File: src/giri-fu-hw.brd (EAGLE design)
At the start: 91.1 x 54.6 mm, 30 parts, among them IC1 ATMEGA168-20P, IC2 7805T, IC3 ULN2003AN, K1 G5V1, K2 G5V1, K3 G5V1, K4 G5V1, K5 G5V1, K6 G5V1, Q1 16MHz

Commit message: Rename inputs and outputs Regenerate dist artifacts
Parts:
- renumbered X10 to SWITCH_1, X11 to SWITCH_2, X12 to SWITCH_3, X13 to SWITCH_4, X14 to SWITCH_5, X15 to SWITCH_6, X16 to 24VAC_IN, X17 to 12VAC_IN
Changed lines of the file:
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@@
 <element name="D4" library="diode" package="DO41-10" value="1N4004" x="17.78" y="20.32" rot="R180"/>
 <element name="C5" library="rcl" package="E35-12" value="" x="24.13" y="34.29" rot="R180"/>
-<element name="X10" library="con-wago-508" package="W237-132" value="" x="81.28" y="5.08" rot="R180">
+<element name="SWITCH_1" library="con-wago-508" package="W237-132" value="" x="81.28" y="5.08" rot="R180">
 <attribute name="OC_NEWARK" value="unknown" x="81.28" y="5.08" size="1.778" layer="27" rot="R180" display="off"/>
 <attribute name="MPN" value="" x="81.28" y="5.08" size="1.778" layer="27" rot="R180" display="off"/>
@@
 <attribute name="OC_FARNELL" value="unknown" x="81.28" y="5.08" size="1.778" layer="27" rot="R180" display="off"/>
 </element>
-<element name="X11" library="con-wago-508" package="W237-132" value="" x="71.12" y="5.08" rot="R180">
+<element name="SWITCH_2" library="con-wago-508" package="W237-132" value="" x="71.12" y="5.08" rot="R180">
 <attribute name="OC_NEWARK" value="unknown" x="71.12" y="5.08" size="1.778" layer="27" rot="R180" display="off"/>
 <attribute name="MPN" value="" x="71.12" y="5.08" size="1.778" layer="27" rot="R180" display="off"/>
@@
 <attribute name="OC_FARNELL" value="unknown" x="71.12" y="5.08" size="1.778" layer="27" rot="R180" display="off"/>
 </element>
-<element name="X12" library="con-wago-508" package="W237-132" value="" x="60.96" y="5.08" rot="R180">
+<element name="SWITCH_3" library="con-wago-508" package="W237-132" value="" x="60.96" y="5.08" rot="R180">
 <attribute name="OC_NEWARK" value="unknown" x="60.96" y="5.08" size="1.778" layer="27" rot="R180" display="off"/>
 <attribute name="MPN" value="" x="60.96" y="5.08" size="1.778" layer="27" rot="R180" display="off"/>
@@
 <attribute name="OC_FARNELL" value="unknown" x="60.96" y="5.08" size="1.778" layer="27" rot="R180" display="off"/>
 </element>
-<element name="X13" library="con-wago-508" package="W237-132" value="" x="50.8" y="5.08" rot="R180">
+<element name="SWITCH_4" library="con-wago-508" package="W237-132" value="" x="50.8" y="5.08" rot="R180">
 <attribute name="OC_NEWARK" value="unknown" x="50.8" y="5.08" size="1.778" layer="27" rot="R180" display="off"/>
 <attribute name="MPN" value="" x="50.8" y="5.08" size="1.778" layer="27" rot="R180" display="off"/>
@@
 <attribute name="OC_FARNELL" value="unknown" x="50.8" y="5.08" size="1.778" layer="27" rot="R180" display="off"/>
 </element>
-<element name="X14" library="con-wago-508" package="W237-132" value="" x="40.64" y="5.08" rot="R180">
+<element name="SWITCH_5" library="con-wago-508" package="W237-132" value="" x="40.64" y="5.08" rot="R180">
 <attribute name="OC_NEWARK" value="unknown" x="40.64" y="5.08" size="1.778" layer="27" rot="R180" display="off"/>
 <attribute name="MPN" value="" x="40.64" y="5.08" size="1.778" layer="27" rot="R180" display="off"/>
@@
 <attribute name="OC_FARNELL" value="unknown" x="40.64" y="5.08" size="1.778" layer="27" rot="R180" display="off"/>
 </element>
-<element name="X15" library="con-wago-508" package="W237-132" value="" x="30.48" y="5.08" rot="R180">
+<element name="SWITCH_6" library="con-wago-508" package="W237-132" value="" x="30.48" y="5.08" rot="R180">
 <attribute name="OC_NEWARK" value="unknown" x="30.48" y="5.08" size="1.778" layer="27" rot="R180" display="off"/>
 <attribute name="MPN" value="" x="30.48" y="5.08" size="1.778" layer="27" rot="R180" display="off"/>
@@
 <attribute name="OC_FARNELL" value="unknown" x="30.48" y="5.08" size="1.778" layer="27" rot="R180" display="off"/>
 </element>
-<element name="X16" library="con-wago-508" package="W237-132" value="" x="20.32" y="5.08" rot="R180">
+<element name="24VAC_IN" library="con-wago-508" package="W237-132" value="" x="20.32" y="5.08" rot="R180">
 <attribute name="OC_NEWARK" value="unknown" x="20.32" y="5.08" size="1.778" layer="27" rot="R180" display="off"/>
 <attribute name="MPN" value="" x="20.32" y="5.08" size="1.778" layer="27" rot="R180" display="off"/>
@@
 <attribute name="OC_FARNELL" value="unknown" x="20.32" y="5.08" size="1.778" layer="27" rot="R180" display="off"/>
 </element>
-<element name="X17" library="con-wago-508" package="W237-132" value="" x="10.16" y="5.08" rot="R180">
+<element name="12VAC_IN" library="con-wago-508" package="W237-132" value="" x="10.16" y="5.08" rot="R180">
 <attribute name="OC_NEWARK" value="unknown" x="10.16" y="5.08" size="1.778" layer="27" rot="R180" display="off"/>
 <attribute name="MPN" value="" x="10.16" y="5.08" size="1.778" layer="27" rot="R180" display="off"/>
@@
 <contactref element="K2" pad="6"/>
 <contactref element="K2" pad="5"/>
-<contactref element="X16" pad="2"/>
+<contactref element="24VAC_IN" pad="2"/>
 <wire x1="27.94" y1="21.59" x2="33.02" y2="21.59" width="1.27" layer="16"/>
 <wire x1="33.02" y1="21.59" x2="34.29" y2="20.32" width="1.27" layer="16"/>
@@
 <contactref element="D4" pad="A"/>
 <contactref element="D1" pad="C"/>
-<contactref element="X17" pad="1"/>
+<contactref element="12VAC_IN" pad="1"/>
 <wire x1="12.7" y1="20.32" x2="12.7" y2="12.7" width="1.27" layer="16"/>
 <wire x1="12.7" y1="12.7" x2="12.7" y2="5.715" width="1.27" layer="16"/>
@@
 <contactref element="D3" pad="A"/>
 <contactref element="D2" pad="C"/>
-<contactref element="X17" pad="2"/>
+<contactref element="12VAC_IN" pad="2"/>
 <wire x1="7.62" y1="24.13" x2="7.62" y2="16.51" width="1.27" layer="16"/>
 <wire x1="7.62" y1="16.51" x2="7.62" y2="5.715" width="1.27" layer="16"/>
 </signal>
 <signal name="N$35">
-<contactref element="X16" pad="1"/>
-<contactref element="X15" pad="1"/>
-<contactref element="X14" pad="1"/>
-<contactref element="X13" pad="1"/>
-<contactref element="X12" pad="1"/>
-<contactref element="X11" pad="1"/>
-<contactref element="X10" pad="1"/>
+<contactref element="24VAC_IN" pad="1"/>
+<contactref element="SWITCH_6" pad="1"/>
+<contactref element="SWITCH_5" pad="1"/>
+<contactref element="SWITCH_4" pad="1"/>
+<contactref element="SWITCH_3" pad="1"/>
+<contactref element="SWITCH_2" pad="1"/>
+<contactref element="SWITCH_1" pad="1"/>
 <wire x1="83.82" y1="5.715" x2="83.82" y2="3.81" width="1.27" layer="16"/>
 <wire x1="83.82" y1="3.81" x2="82.55" y2="2.54" width="1.27" layer="16"/>
@@
 </signal>
 <signal name="N$28">
-<contactref element="X10" pad="2"/>
+<contactref element="SWITCH_1" pad="2"/>
 <contactref element="K1" pad="10"/>
 <wire x1="78.74" y1="11.43" x2="78.74" y2="5.715" width="1.27" layer="16"/>
 </signal>
 <signal name="N$29">
-<contactref element="X11" pad="2"/>
+<contactref element="SWITCH_2" pad="2"/>
 <contactref element="K2" pad="10"/>
 <wire x1="68.58" y1="11.43" x2="68.58" y2="5.715" width="1.27" layer="16"/>
 </signal>
 <signal name="N$30">
-<contactref element="X12" pad="2"/>
+<contactref element="SWITCH_3" pad="2"/>
 <contactref element="K3" pad="10"/>
 <wire x1="58.42" y1="11.43" x2="58.42" y2="5.715" width="1.27" layer="16"/>
 </signal>
 <signal name="N$31">
-<contactref element="X13" pad="2"/>
+<contactref element="SWITCH_4" pad="2"/>
 <contactref element="K4" pad="10"/>
 <wire x1="48.26" y1="11.43" x2="48.26" y2="5.715" width="1.27" layer="16"/>
 </signal>
 <signal name="N$32">
-<contactref element="X14" pad="2"/>
+<contactref element="SWITCH_5" pad="2"/>
 <contactref element="K5" pad="10"/>
 <wire x1="38.1" y1="11.43" x2="38.1" y2="5.715" width="1.27" layer="16"/>
 </signal>
 <signal name="N$33">
-<contactref element="X15" pad="2"/>
+<contactref element="SWITCH_6" pad="2"/>
 <contactref element="K6" pad="10"/>
 <wire x1="27.94" y1="11.43" x2="27.94" y2="5.715" width="1.27" layer="16"/>

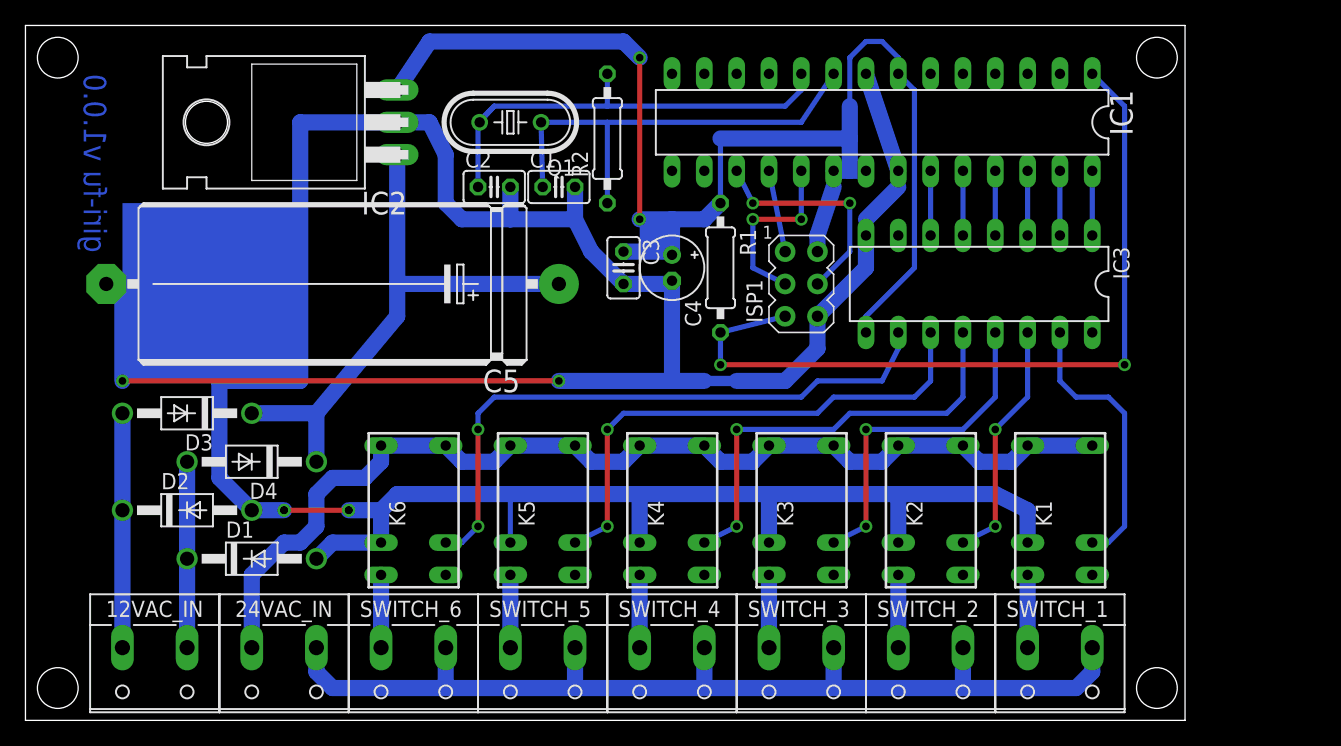
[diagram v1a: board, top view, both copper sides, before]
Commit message: Change the relay driver endpoint from ground to vcc
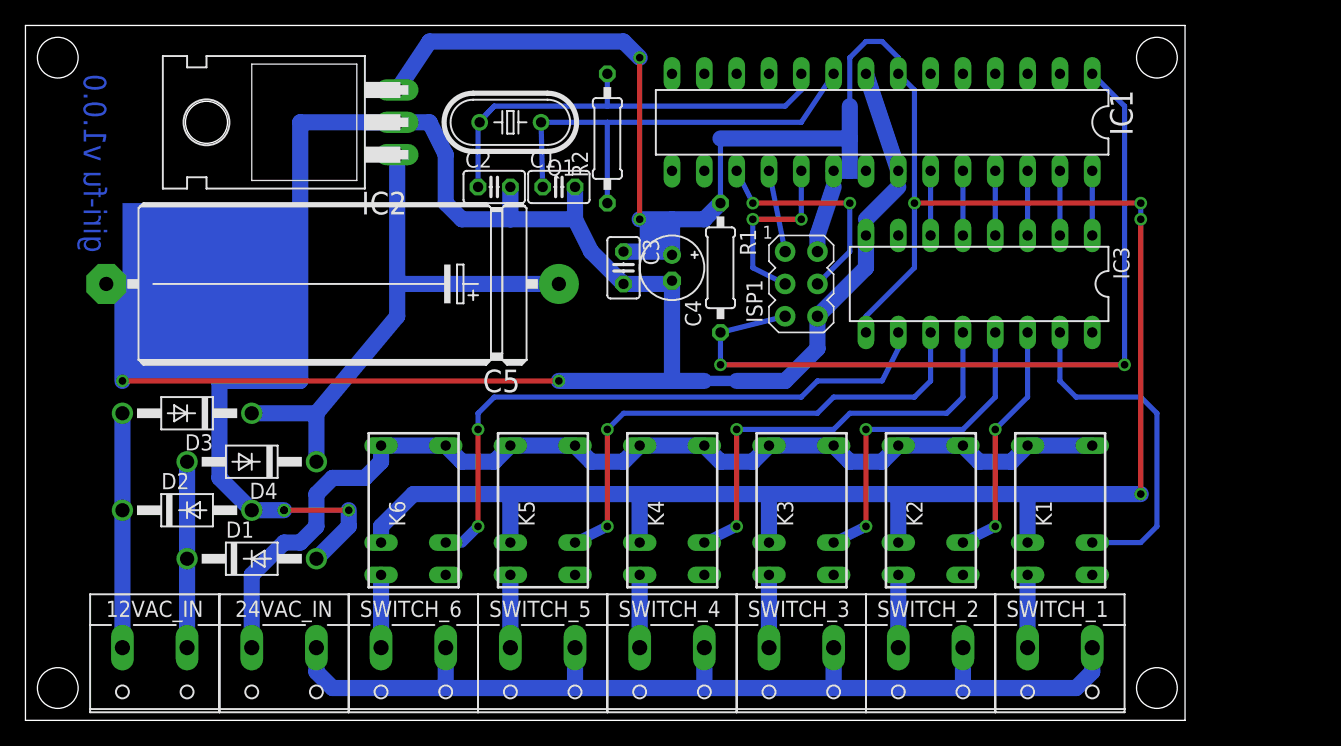
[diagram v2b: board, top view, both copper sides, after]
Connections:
- removed net VCC: C3.1, C4.+, IC1.20, IC1.21, IC1.7, IC2.3, IC3.9, ISP1.2, R1.1
- new net N$8: C3.1, C4.+, IC1.20, IC1.21, IC1.7, IC2.3, IC3.9, ISP1.2, K1.9, K2.9, K3.9, K4.9, K5.9, K6.9, R1.1
- net GND: no longer K1.9, K2.9, K3.9, K4.9, K5.9, K6.9
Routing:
- net N$8: track 0.00 -> 231.3 mm, vias 0 -> 6
- net VCC: track 109.6 -> 0.00 mm, vias 2 -> 0
- net GND: track 276.5 -> 201.3 mm
- net N$20: track 21.9 -> 27.0 mm
